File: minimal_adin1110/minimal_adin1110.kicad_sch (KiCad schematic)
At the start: 70 parts, among them J1 CLP-112-02-G-D-BE, J2 CLP-102-02-G-D-BE, J3 CLP-102-02-G-D-BE, J4 CLP-102-02-G-D-BE, J5 CLP-102-02-G-D-BE, U1 ADIN1110CCPZ, Y1 FA-128 25.0000MF20X-K0

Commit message: Update subproject commit for KiCAD Symbol Generator
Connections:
- net DATA_AND_POWER_N: no longer J5.3
- net DATA_AND_POWER_P: now also J5.3; no longer J5.2, J5.4
- net GND: now also J5.2, J5.4
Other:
- moved on the sheet: J5
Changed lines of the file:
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@@
 	)
 	(junction
-		(at 330.2 142.24)
-		(diameter 0)
-		(color 0 0 0 0)
-	)
-	(junction
 		(at 198.12 86.36)
 		(diameter 0)
@@
 	)
 	(junction
+		(at 350.52 149.86)
+		(diameter 0)
+		(color 0 0 0 0)
+	)
+	(junction
 		(at 278.13 40.64)
 		(diameter 0)
@@
 	)
 	(junction
-		(at 330.2 154.94)
-		(diameter 0)
-		(color 0 0 0 0)
-	)
-	(junction
 		(at 172.72 180.34)
 		(diameter 0)
@@
 	(wire
 		(pts
-			(xy 330.2 142.24) (xy 328.93 142.24)
+			(xy 109.22 142.24) (xy 106.68 142.24)
 		)
 		(stroke
@@
 	(wire
 		(pts
-			(xy 109.22 142.24) (xy 106.68 142.24)
+			(xy 303.53 157.48) (xy 307.34 157.48)
 		)
 		(stroke
@@
 	(wire
 		(pts
-			(xy 303.53 157.48) (xy 307.34 157.48)
+			(xy 109.22 149.86) (xy 106.68 149.86)
 		)
 		(stroke
@@
 	(wire
 		(pts
-			(xy 109.22 149.86) (xy 106.68 149.86)
+			(xy 254 48.26) (xy 254 46.99)
 		)
 		(stroke
@@
 	(wire
 		(pts
-			(xy 254 48.26) (xy 254 46.99)
+			(xy 106.68 132.08) (xy 106.68 134.62)
 		)
 		(stroke
@@
 	(wire
 		(pts
-			(xy 106.68 132.08) (xy 106.68 134.62)
+			(xy 177.8 66.04) (xy 177.8 81.28)
 		)
 		(stroke
@@
 	(wire
 		(pts
-			(xy 177.8 66.04) (xy 177.8 81.28)
+			(xy 347.98 149.86) (xy 350.52 149.86)
 		)
 		(stroke
@@
 	(wire
 		(pts
+			(xy 330.2 147.32) (xy 337.82 147.32)
+		)
+		(stroke
+			(width 0)
+			(type default)
+		)
+	)
+	(wire
+		(pts
 			(xy 223.52 111.76) (xy 228.6 111.76)
 		)
@@
 	(wire
 		(pts
+			(xy 347.98 147.32) (xy 350.52 147.32)
+		)
+		(stroke
+			(width 0)
+			(type default)
+		)
+	)
+	(wire
+		(pts
 			(xy 152.4 170.18) (xy 152.4 180.34)
 		)
@@
 	(wire
 		(pts
-			(xy 331.47 154.94) (xy 331.47 153.67)
+			(xy 330.2 149.86) (xy 330.2 162.56)
 		)
 		(stroke
@@
 	(wire
 		(pts
-			(xy 330.2 134.62) (xy 330.2 142.24)
+			(xy 350.52 151.13) (xy 350.52 149.86)
 		)
 		(stroke
@@
 	(wire
 		(pts
-			(xy 330.2 154.94) (xy 331.47 154.94)
-		)
-		(stroke
-			(width 0)
-			(type default)
-		)
-	)
-	(wire
-		(pts
 			(xy 271.78 91.44) (xy 271.78 93.98)
 		)
@@
 	(wire
 		(pts
-			(xy 330.2 154.94) (xy 330.2 162.56)
-		)
-		(stroke
-			(width 0)
-			(type default)
-		)
-	)
-	(wire
-		(pts
 			(xy 152.4 190.5) (xy 152.4 193.04)
 		)
@@
 	(wire
 		(pts
-			(xy 330.2 142.24) (xy 331.47 142.24)
-		)
-		(stroke
-			(width 0)
-			(type default)
-		)
-	)
-	(wire
-		(pts
 			(xy 254 76.2) (xy 254 74.93)
 		)
@@
 	(wire
 		(pts
-			(xy 328.93 143.51) (xy 328.93 142.24)
-		)
-		(stroke
-			(width 0)
-			(type default)
-		)
-	)
-	(wire
-		(pts
 			(xy 280.67 69.85) (xy 280.67 68.58)
 		)
@@
 	(wire
 		(pts
-			(xy 331.47 142.24) (xy 331.47 143.51)
+			(xy 330.2 134.62) (xy 330.2 147.32)
 		)
 		(stroke
@@
 	(wire
 		(pts
-			(xy 328.93 154.94) (xy 330.2 154.94)
-		)
-		(stroke
-			(width 0)
-			(type default)
-		)
-	)
-	(wire
-		(pts
 			(xy 198.12 81.28) (xy 198.12 86.36)
 		)
@@
 	(wire
 		(pts
-			(xy 328.93 153.67) (xy 328.93 154.94)
-		)
-		(stroke
-			(width 0)
-			(type default)
-		)
-	)
-	(wire
-		(pts
 			(xy 271.78 134.62) (xy 281.94 134.62)
 		)
@@
 	(wire
 		(pts
+			(xy 330.2 149.86) (xy 337.82 149.86)
+		)
+		(stroke
+			(width 0)
+			(type default)
+		)
+	)
+	(wire
+		(pts
 			(xy 226.06 106.68) (xy 228.6 106.68)
 		)
@@
 	(wire
 		(pts
+			(xy 350.52 147.32) (xy 350.52 149.86)
+		)
+		(stroke
+			(width 0)
+			(type default)
+		)
+	)
+	(wire
+		(pts
 			(xy 220.98 68.58) (xy 220.98 73.66)
 		)
@@
 	(symbol
 		(lib_id "UNITED_CONNECTORS_DATA_BASE:J_CLP-102-02-G-D-BE")
-		(at 330.2 148.59 90)
+		(at 342.9 148.59 0)
+		(mirror x)
 		(unit 1)
 		(exclude_from_sim no)
@@
 		(on_board yes)
 		(dnp no)
-		(fields_autoplaced yes)
 		(property "Reference" "J5"
-			(at 335.28 147.3199 90)
+			(at 342.9 139.7 0)
 			(effects
 				(font
 					(size 1.27 1.27)
 				)
-				(justify right)
 			)
 		)
 		(property "Value" "CLP-102-02-G-D-BE"
-			(at 335.28 149.8599 90)
+			(at 342.9 142.24 0)
 			(effects
 				(font
 					(size 1.27 1.27)
 				)
-				(justify right)
 			)
 		)
 		(property "Footprint" "connector_footprints:CLP-102-02-G-D-BE"
-			(at 337.82 143.51 0)
+			(at 347.98 140.97 0)
 			(show_name yes)
 			(effects
@@
 		)
 		(property "Datasheet" "https://suddendocs.samtec.com/catalog_english/clp_sm.pdf?_gl=1*1y4jlr9*_gcl_au*MTM0MTYyNTQ5MS4xNzM2MDk5MTUz*_ga*MTYxNDYyMTQ0Mi4xNzM2MDk5MTUz*_ga_3KFNZC07WW*MTczNjY4MDQ4OS4xNS4xLjE3MzY2ODEzNzcuNjAuMC4w"
-			(at 340.36 143.51 0)
+			(at 347.98 138.43 0)
 			(show_name yes)
 			(effects
@@
 		)
 		(property "Description" "Samtec CLP-1xx-02-G-D-BE series,  2 positions connector,  1.27 mm pitch,  Black,  Vertical mounting,  5.2 A,  300 V,  Through Hole,  Tin plated"
-			(at 342.9 143.51 0)
+			(at 347.98 135.89 0)
 			(show_name yes)
 			(effects
@@
 		)
 		(property "Color" "Black"
-			(at 345.44 143.51 0)
+			(at 347.98 133.35 0)
 			(show_name yes)
 			(effects
@@
 		)
 		(property "Contact Plating" "Tin"
-			(at 347.98 143.51 0)
+			(at 347.98 130.81 0)
 			(show_name yes)
 			(effects
@@
 		)
 		(property "Current Rating (A)" "5.2"
-			(at 350.52 143.51 0)
+			(at 347.98 128.27 0)
 			(show_name yes)
 			(effects
@@
 		)
 		(property "MPN" "CLP-102-02-G-D-BE"
-			(at 353.06 143.51 0)
+			(at 347.98 125.73 0)
 			(show_name yes)
 			(effects
@@
 		)
 		(property "Manufacturer" "Samtec"
-			(at 355.6 143.51 0)
+			(at 347.98 123.19 0)
 			(show_name yes)
 			(effects
@@
 		)
 		(property "Mounting Angle" "Vertical"
-			(at 358.14 143.51 0)
+			(at 347.98 120.65 0)
 			(show_name yes)
 			(effects
@@
 		)
 		(property "Mounting Style" "Through Hole"
-			(at 360.68 143.51 0)
+			(at 347.98 118.11 0)
 			(show_name yes)
 			(effects
@@
 		)
 		(property "Number of Rows" "2"
-			(at 363.22 143.51 0)
+			(at 347.98 115.57 0)
 			(show_name yes)
 			(effects
@@
 		)
 		(property "Pin Count" "2"
-			(at 365.76 143.51 0)
+			(at 347.98 113.03 0)
 			(show_name yes)
 			(effects
@@
 		)
 		(property "Pitch (mm)" "1.27"
-			(at 368.3 143.51 0)
+			(at 347.98 110.49 0)
 			(show_name yes)
 			(effects
@@
 		)
 		(property "Series" "CLP-1xx-02-G-D-BE"
-			(at 370.84 143.51 0)
+			(at 347.98 107.95 0)
 			(show_name yes)
 			(effects
@@
 		)
 		(property "Symbol Name" "J_CLP-102-02-G-D-BE"
-			(at 373.38 143.51 0)
+			(at 347.98 105.41 0)
 			(show_name yes)
 			(effects
@@
 		)
 		(property "Trustedparts Search" "https://www.trustedparts.com/en/search/CLP-102-02-G-D-BE"
-			(at 375.92 143.51 0)
+			(at 347.98 102.87 0)
 			(show_name yes)
 			(effects
@@
 		)
 		(property "Voltage Rating (V)" "300"
-			(at 378.46 143.51 0)
+			(at 347.98 100.33 0)
 			(show_name yes)
 			(effects
@@
 					(unit 1)
 				)
+			)
+		)
+	)
+	(symbol
+		(lib_id "power:GND")
+		(at 350.52 151.13 0)
+		(unit 1)
+		(exclude_from_sim no)
+		(in_bom yes)
+		(on_board yes)
+		(dnp no)
+		(fields_autoplaced yes)
+		(property "Reference" "#PWR22"
+			(at 350.52 157.48 0)
+			(effects
+				(font
+					(size 1.27 1.27)
+				)
+				(hide yes)
+			)
+		)
+		(property "Value" "GND"
+			(at 350.52 156.21 0)
+			(effects
+				(font
+					(size 1.27 1.27)
+				)
+			)
+		)
+		(property "Footprint" ""
+			(at 350.52 151.13 0)
+			(effects
+				(font
+					(size 1.27 1.27)
+				)
+				(hide yes)
+			)
+		)
+		(property "Datasheet" ""
+			(at 350.52 151.13 0)
+			(effects
+				(font
+					(size 1.27 1.27)
+				)
+				(hide yes)
+			)
+		)
+		(property "Description" "Power symbol creates a global label with name \"GND\" , ground"
+			(at 350.52 151.13 0)
+			(effects
+				(font
+					(size 1.27 1.27)
+				)
+				(hide yes)
+			)
+		)
+		(pin "1"
+		)
+		(instances
+			(project "minimal_adin1110"
+				(path "/26ddf1b8-aee4-468d-a26c-7bd63f3a2989"
+					(reference "#PWR22")
+					(unit 1)
+				)

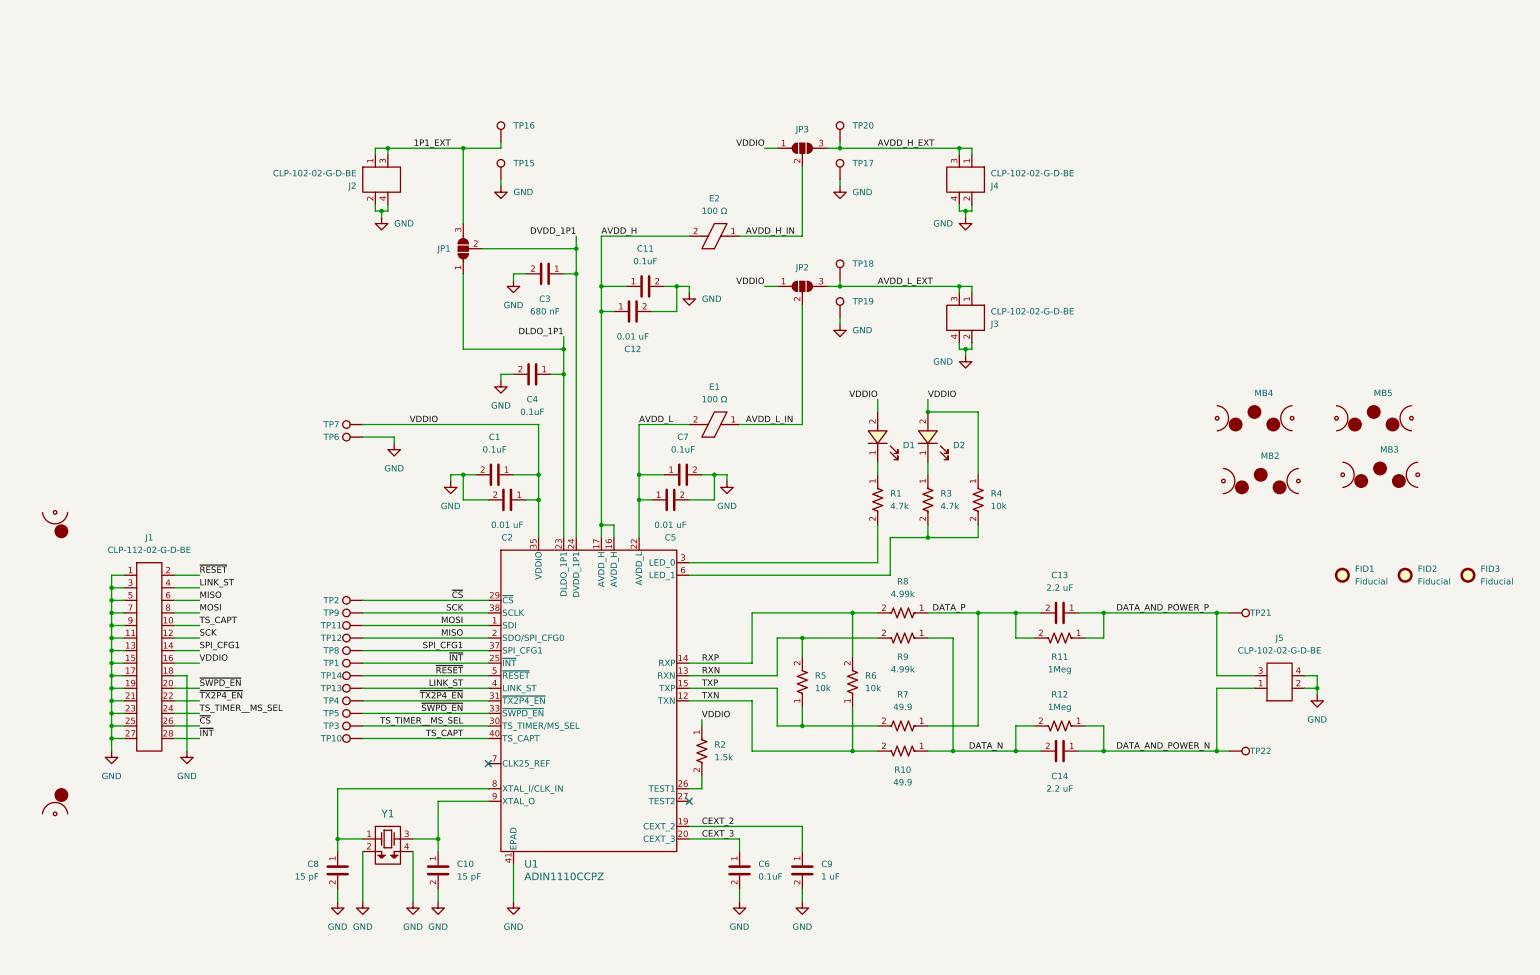
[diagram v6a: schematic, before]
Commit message: Update KiCAD subproject commit and adjust pad dimensions
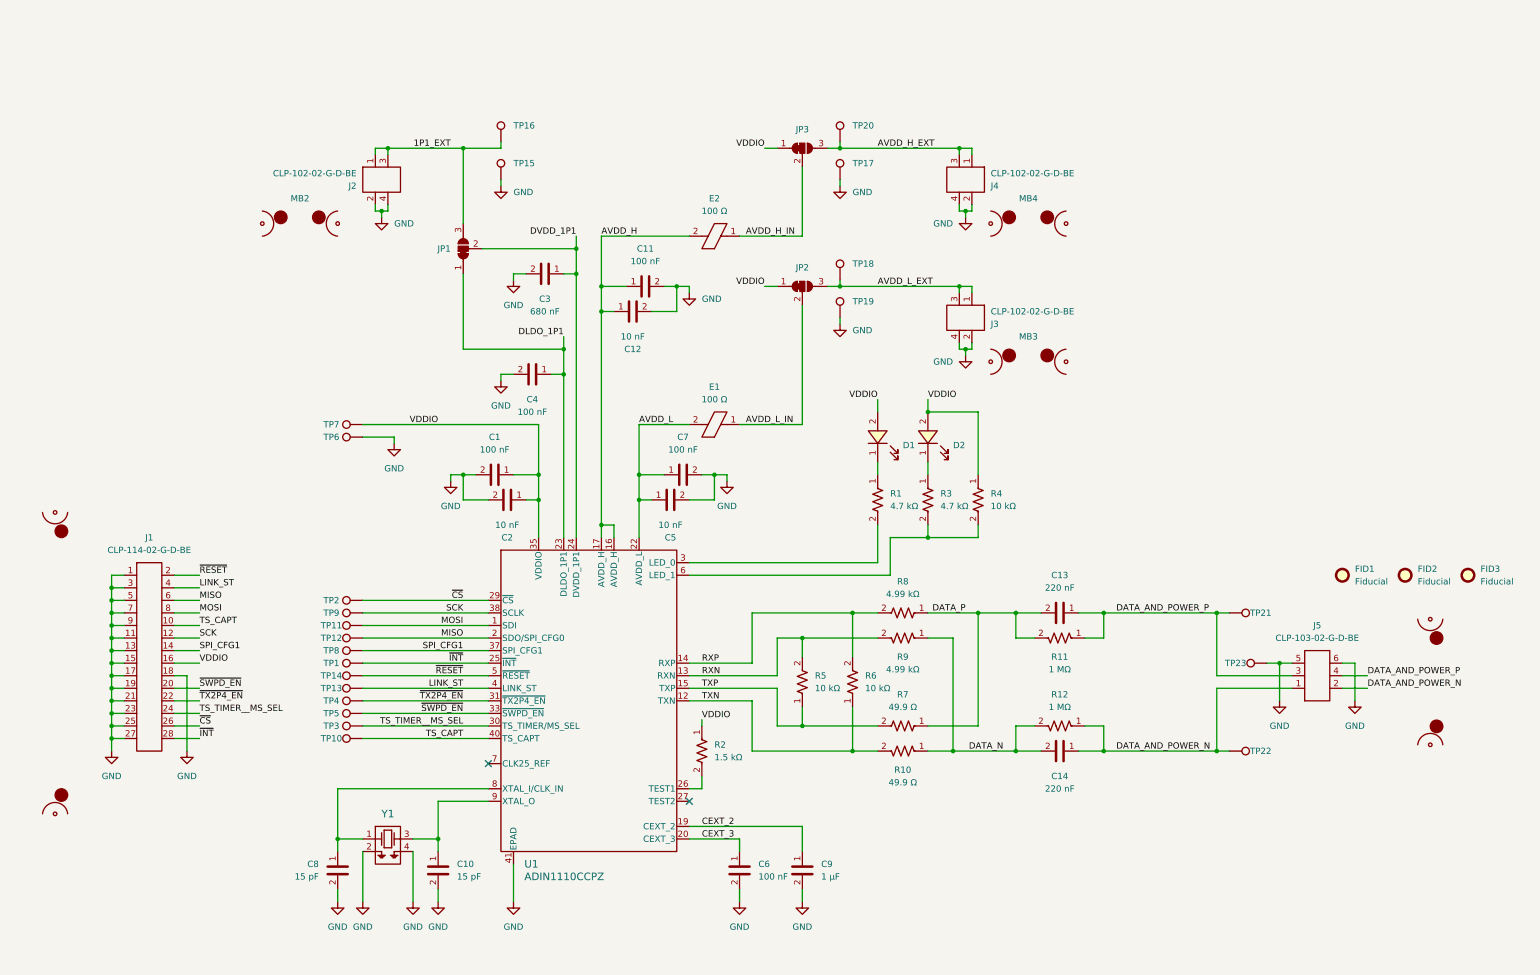
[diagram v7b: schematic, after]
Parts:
- added TP23: TestPoint, test_point_footprints:TestPoint_THTPad_Castelated, symbol UNITED_TEST_POINTS:TestPoint_Castelated
- C1, C11, C4, C6, C7: value 0.1uF -> 100 nF; 3dviewer Link (none) -> https://3dviewer.net/index.html#model=https://github.com/io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; Capacitor Type (none) -> Ceramic
- C10, C3, C8: 3dviewer Link (none) -> https://3dviewer.net/index.html#model=https://github.com/io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; Capacitor Type (none) -> Ceramic
- C12, C2, C5: value 0.01 uF -> 10 nF; 3dviewer Link (none) -> https://3dviewer.net/index.html#model=https://github.com/io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; Capacitor Type (none) -> Ceramic
- C13, C14: value 2.2 uF -> 220 nF; 3dviewer Link (none) -> https://3dviewer.net/index.html#model=https://github.com/io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; Capacitor Type (none) -> Ceramic
- C9: value 1 uF -> 1 µF; 3dviewer Link (none) -> https://3dviewer.net/index.html#model=https://github.com/io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; Capacitor Type (none) -> Ceramic
- D1, D2: value APHHS1005CGCK -> 1.8 V
- J1: value CLP-112-02-G-D-BE -> CLP-114-02-G-D-BE; Mounting Style Through Hole -> Surface Mount
- J2, J3, J4: Mounting Style Through Hole -> Surface Mount
- J5: value CLP-102-02-G-D-BE -> CLP-103-02-G-D-BE; footprint connector_footprints:CLP-102-02-G-D-BE -> connector_footprints:CLP-103-02-G-D-BE; symbol UNITED_CONNECTORS_DATA_BASE:J_CLP-102-02-G-D-BE -> UNITED_CONNECTORS_DATA_BASE:J_CLP-103-02-G-D-BE; MPN CLP-102-02-G-D-BE -> CLP-103-02-G-D-BE; Mounting Style Through Hole -> Surface Mount; Pin Count 2 -> 3; Symbol Name J_CLP-102-02-G-D-BE -> J_CLP-103-02-G-D-BE; Trustedparts Search https://www.trustedparts.com/en/search/CLP-102-02-G-D-BE -> https://www.trustedparts.com/en/search/CLP-103-02-G-D-BE
- JP1, JP2, JP3: footprint solder_jumper_footprints:SolderJumper-3_P1.3mm_Open_RoundedPad1.0x1.5mm_NumberLabels -> solder_jumper_footprints:SolderJumper-3_P1.3mm_Bridged_1_2_RoundedPad1.0x1.5mm_NumberLabels; symbol UNITED_SOLDER_JUMPERS:SolderJumper_3_Open -> UNITED_SOLDER_JUMPERS:SolderJumper_3_Bridged_1_2
- MB5: footprint mouse_bite_footprints:mouse-bite-midle-50mil-200mil -> mouse_bite_footprints:mouse-bite-midle-50mil-250mil; symbol UNITED_MOUSE_BITES_DATA_BASE:mouse-bite-midle-50mil-200mil -> UNITED_MOUSE_BITES_DATA_BASE:mouse-bite-midle-50mil-250mil
- R1, R3: value 4.7k -> 4.7 kΩ; 3dviewer Link (none) -> https://3dviewer.net/index.html#model=https://github.com/io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; Component Type (none) -> Resistor
- R10, R7: value 49.9 -> 49.9 Ω; 3dviewer Link (none) -> https://3dviewer.net/index.html#model=https://github.com/io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; Component Type (none) -> Resistor
- R11, R12: value 1Meg -> 1 MΩ; 3dviewer Link (none) -> https://3dviewer.net/index.html#model=https://github.com/io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; Component Type (none) -> Resistor
- R2: value 1.5k -> 1.5 kΩ; 3dviewer Link (none) -> https://3dviewer.net/index.html#model=https://github.com/io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; Component Type (none) -> Resistor
- R4, R5, R6: value 10k -> 10 kΩ; 3dviewer Link (none) -> https://3dviewer.net/index.html#model=https://github.com/io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; Component Type (none) -> Resistor
- R8, R9: value 4.99k -> 4.99 kΩ; 3dviewer Link (none) -> https://3dviewer.net/index.html#model=https://github.com/io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; Component Type (none) -> Resistor
- Y1: value FA-128 25.0000MF20X-K0 -> 25.0000MHz
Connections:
- net DATA_AND_POWER_N: now also J5.2
- net DATA_AND_POWER_P: now also J5.4
- net GND: now also J5.5, J5.6, TP23.1; no longer J5.2, J5.4

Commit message: Update subproject commit for KiCAD Symbol Generator
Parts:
- added D3, D4: 3.3 V, diode_footprints:SOD323, symbol UNITED_DIODES_DATA_BASE:D_SP4020-01FTG
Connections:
- net DATA_AND_POWER_N: now also D4.1
- net DATA_AND_POWER_P: now also D3.1
- net GND: now also D3.2, D4.2
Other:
- moved on the sheet: FID1, FID2, FID3, J5, TP21, TP22, TP23
